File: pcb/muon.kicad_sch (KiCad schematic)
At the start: 55 parts, among them J1 Debug Pins, J2 USB_C_Receptacle_USB2.0, SW1 Kailh Hotswap, SW2 Kailh Hotswap, SW3 Reset, SW7 Kailh Hotswap, U1 SRV05-4, U2 TLV75533PDBVR, U3 RP2040, U4 W25Q80DVSSIG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

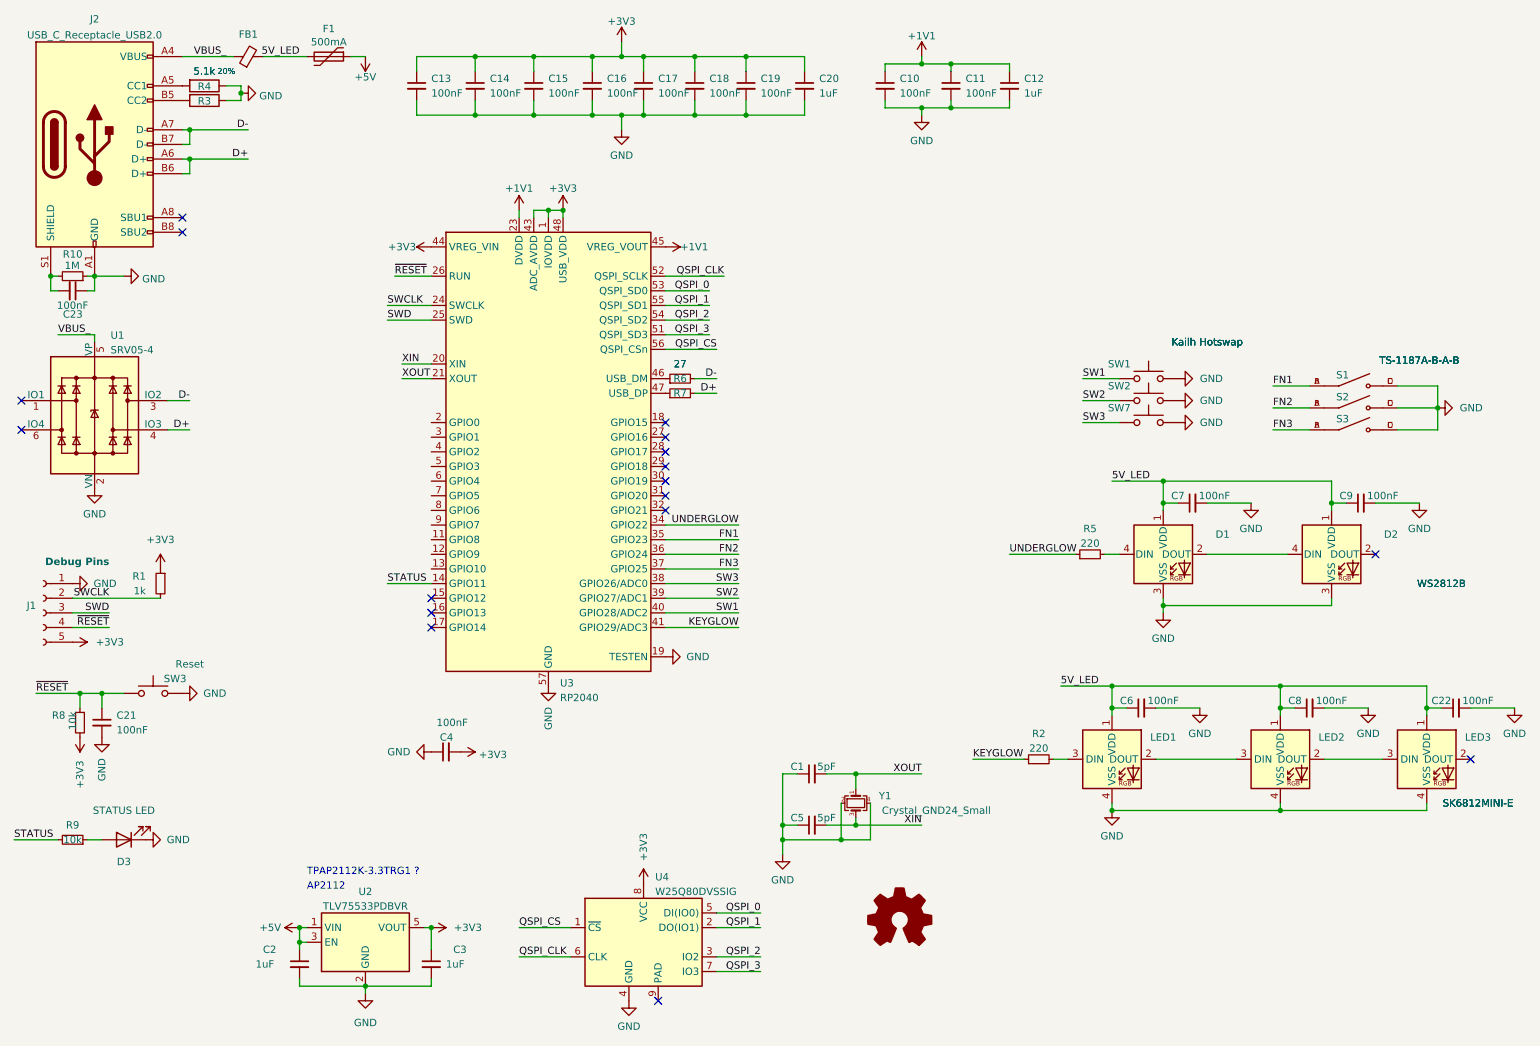
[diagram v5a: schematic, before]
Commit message: update page titles, use an actual Ferrite Bead (has just been a 0ohm resistor till now
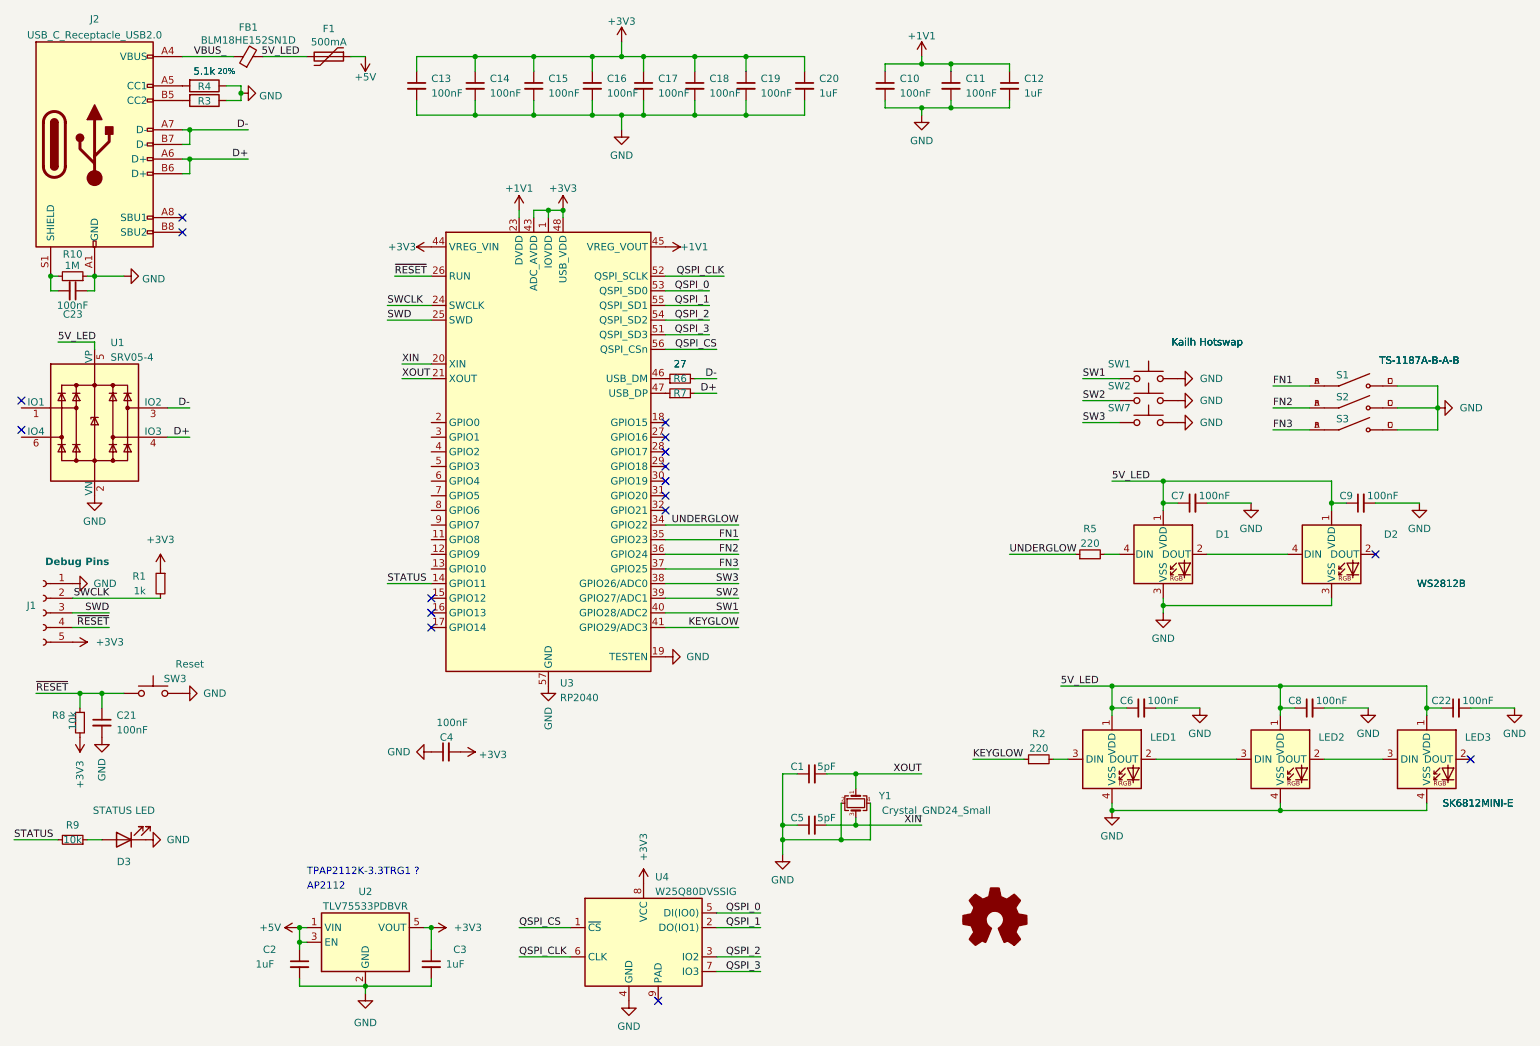
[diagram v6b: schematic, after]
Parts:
- FB1: value ~ -> BLM18HE152SN1D; footprint Inductor_SMD:L_0402_1005Metric -> Inductor_SMD:L_0603_1608Metric
- J1: now left out of the parts list
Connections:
- net 5V_LED: now also U1.5 (VP)
- net VBUS_: no longer U1.5 (VP)
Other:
- company: (none) -> Dekanova LLC
- title: (none) -> Muon
- moved on the sheet: U1
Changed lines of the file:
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@@
 (kicad_sch (version 20211123) (generator eeschema)
   (paper "A4")
+  (title_block
+    (title "Muon")
+    (date "2022-11-13")
+    (rev "v0.6")
+    (company "Dekanova LLC")
+    (comment 1 "           CERN OHL v2 S")
+  )
   (junction (at 119.38 34.29) (diameter 0) (color 0 0 0 0)
   )
@@
     (stroke (width 0) (type default) (color 0 0 0 0))
   )
-  (wire (pts (xy 27.94 73.66) (xy 27.94 72.39))
+  (wire (pts (xy 27.94 74.93) (xy 27.94 73.66))
     (stroke (width 0) (type default) (color 0 0 0 0))
   )
@@
     (stroke (width 0) (type default) (color 0 0 0 0))
   )
-  (wire (pts (xy 40.64 88.9) (xy 44.45 88.9))
+  (wire (pts (xy 40.64 90.17) (xy 44.45 90.17))
     (stroke (width 0) (type default) (color 0 0 0 0))
   )
@@
     (stroke (width 0) (type default) (color 0 0 0 0))
   )
-  (wire (pts (xy 21.59 72.39) (xy 27.94 72.39))
+  (wire (pts (xy 21.59 73.66) (xy 27.94 73.66))
     (stroke (width 0) (type default) (color 0 0 0 0))
   )
@@
     (stroke (width 0) (type default) (color 0 0 0 0))
   )
-  (wire (pts (xy 40.64 83.82) (xy 44.45 83.82))
+  (wire (pts (xy 40.64 85.09) (xy 44.45 85.09))
     (stroke (width 0) (type default) (color 0 0 0 0))
   )
@@
     (effects (font (size 1.27 1.27)) (justify right bottom))
   )
-  (label "VBUS_" (at 21.59 72.39 0)
+  (label "5V_LED" (at 21.59 73.66 0)
     (effects (font (size 1.27 1.27)) (justify left bottom))
   )
@@
     (effects (font (size 1.27 1.27)) (justify right bottom))
   )
-  (label "D-" (at 44.45 83.82 180)
+  (label "D-" (at 44.45 85.09 180)
     (effects (font (size 1.27 1.27)) (justify right bottom))
   )
@@
     (effects (font (size 1.27 1.27)) (justify left bottom))
   )
-  (label "D+" (at 44.45 88.9 180)
+  (label "D+" (at 44.45 90.17 180)
     (effects (font (size 1.27 1.27)) (justify right bottom))
   )
@@
     (pin "2")
   )
-  (symbol (lib_id "Graphic:Logo_Open_Hardware_Small") (at 167.64 173.99 0) (unit 1)
-    (in_bom yes) (on_board yes) (fields_autoplaced)
-    (property "Reference" "#LOGO1" (id 0) (at 167.64 167.005 0)
-      (effects (font (size 1.27 1.27)) hide)
-    )
-    (property "Value" "Logo_Open_Hardware_Small" (id 1) (at 167.64 179.705 0)
-      (effects (font (size 1.27 1.27)) hide)
-    )
-    (property "Footprint" "" (id 2) (at 167.64 173.99 0)
-      (effects (font (size 1.27 1.27)) hide)
-    )
-    (property "Datasheet" "~" (id 3) (at 167.64 173.99 0)
+  (symbol (lib_id "Graphic:Logo_Open_Hardware_Small") (at 184.15 173.99 0) (unit 1)
+    (in_bom yes) (on_board yes) (fields_autoplaced)
+    (property "Reference" "#LOGO1" (id 0) (at 184.15 167.005 0)
+      (effects (font (size 1.27 1.27)) hide)
+    )
+    (property "Value" "Logo_Open_Hardware_Small" (id 1) (at 184.15 179.705 0)
+      (effects (font (size 1.27 1.27)) hide)
+    )
+    (property "Footprint" "" (id 2) (at 184.15 173.99 0)
+      (effects (font (size 1.27 1.27)) hide)
+    )
+    (property "Datasheet" "~" (id 3) (at 184.15 173.99 0)
       (effects (font (size 1.27 1.27)) hide)
     )
@@
     (pin "2")
   )
-  (symbol (lib_id "marbastlib-various:SRV05-4") (at 27.94 86.36 0) (unit 1)
-    (in_bom yes) (on_board yes) (fields_autoplaced)
-    (property "Reference" "U1" (id 0) (at 30.7087 72.5002 0)
-      (effects (font (size 1.27 1.27)) (justify left))
-    )
-    (property "Value" "SRV05-4" (id 1) (at 30.7087 75.0371 0)
-      (effects (font (size 1.27 1.27)) (justify left))
-    )
-    (property "Footprint" "marbastlib-various:SOT-23-6-routable" (id 2) (at 45.72 97.79 0)
-      (effects (font (size 1.27 1.27)) hide)
-    )
-    (property "Datasheet" "http://www.onsemi.com/pub/Collateral/SRV05-4-D.PDF" (id 3) (at 27.94 86.36 0)
+  (symbol (lib_id "marbastlib-various:SRV05-4") (at 27.94 87.63 0) (unit 1)
+    (in_bom yes) (on_board yes) (fields_autoplaced)
+    (property "Reference" "U1" (id 0) (at 30.7087 73.7702 0)
+      (effects (font (size 1.27 1.27)) (justify left))
+    )
+    (property "Value" "SRV05-4" (id 1) (at 30.7087 76.3071 0)
+      (effects (font (size 1.27 1.27)) (justify left))
+    )
+    (property "Footprint" "marbastlib-various:SOT-23-6-routable" (id 2) (at 45.72 99.06 0)
+      (effects (font (size 1.27 1.27)) hide)
+    )
+    (property "Datasheet" "http://www.onsemi.com/pub/Collateral/SRV05-4-D.PDF" (id 3) (at 27.94 87.63 0)
       (effects (font (size 1.27 1.27)) hide)
     )
@@
   )
   (symbol (lib_id "Connector:Conn_01x05_Female") (at 19.05 120.65 0) (mirror y) (unit 1)
-    (in_bom yes) (on_board yes)
+    (in_bom no) (on_board yes)
     (property "Reference" "J1" (id 0) (at 17.78 119.3799 0)
       (effects (font (size 1.27 1.27)) (justify left))
@@
   (symbol (lib_id "Device:Ferrite_Bead_Small") (at 54.61 24.13 90) (unit 1)
     (in_bom yes) (on_board yes)
-    (property "Reference" "FB1" (id 0) (at 54.61 20.265 90))
-    (property "Value" "~" (id 1) (at 54.61 21.2937 90))
-    (property "Footprint" "Inductor_SMD:L_0402_1005Metric" (id 2) (at 54.61 25.908 90)
+    (property "Reference" "FB1" (id 0) (at 54.61 19.05 90))
+    (property "Value" "BLM18HE152SN1D" (id 1) (at 54.61 21.2937 90))
+    (property "Footprint" "Inductor_SMD:L_0603_1608Metric" (id 2) (at 54.61 25.908 90)
       (effects (font (size 1.27 1.27)) hide)
     )
@@
     (pin "2")
   )
-  (symbol (lib_id "power:GND") (at 27.94 99.06 0) (unit 1)
-    (in_bom yes) (on_board yes) (fields_autoplaced)
-    (property "Reference" "#PWR0102" (id 0) (at 27.94 105.41 0)
-      (effects (font (size 1.27 1.27)) hide)
-    )
-    (property "Value" "GND" (id 1) (at 27.94 103.5034 0))
-    (property "Footprint" "" (id 2) (at 27.94 99.06 0)
-      (effects (font (size 1.27 1.27)) hide)
-    )
-    (property "Datasheet" "" (id 3) (at 27.94 99.06 0)
+  (symbol (lib_id "power:GND") (at 27.94 100.33 0) (unit 1)
+    (in_bom yes) (on_board yes) (fields_autoplaced)
+    (property "Reference" "#PWR0102" (id 0) (at 27.94 106.68 0)
+      (effects (font (size 1.27 1.27)) hide)
+    )
+    (property "Value" "GND" (id 1) (at 27.94 104.7734 0))
+    (property "Footprint" "" (id 2) (at 27.94 100.33 0)
+      (effects (font (size 1.27 1.27)) hide)
+    )
+    (property "Datasheet" "" (id 3) (at 27.94 100.33 0)
       (effects (font (size 1.27 1.27)) hide)
     )
@@
     )
     (path "/57a1ad18-9c20-45df-8d99-3eb1001c4a85"
-      (reference "FB1") (unit 1) (value "~") (footprint "Inductor_SMD:L_0402_1005Metric")
+      (reference "FB1") (unit 1) (value "BLM18HE152SN1D") (footprint "Inductor_SMD:L_0603_1608Metric")
     )
     (path "/0ff39221-c92f-4e4d-a18b-e53c9e597d78"
